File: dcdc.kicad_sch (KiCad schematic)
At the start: 72 parts, among them U2 LD1117S50TR_SOT223, U3 LD1117S33TR_SOT223, U4 ISU0205S15, U5 ISU0205S15, U6 LT3032, U7 LT3032

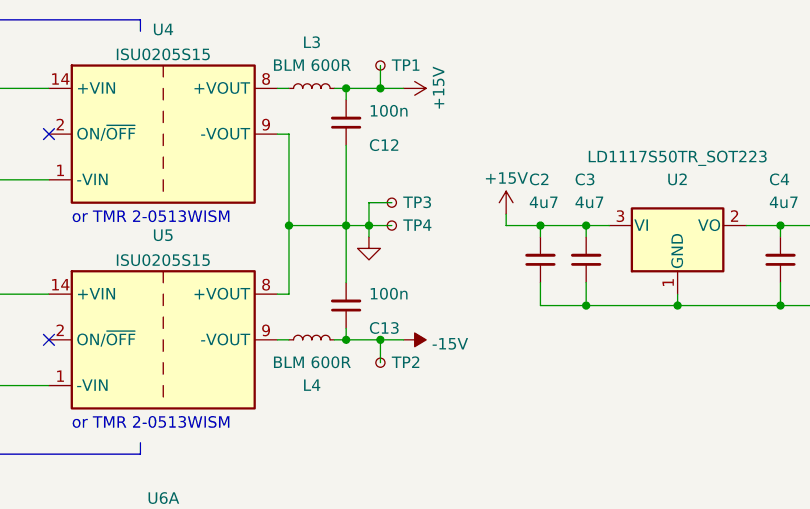
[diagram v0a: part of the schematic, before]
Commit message: Add more testpoints, make DRDY optionally open collector.
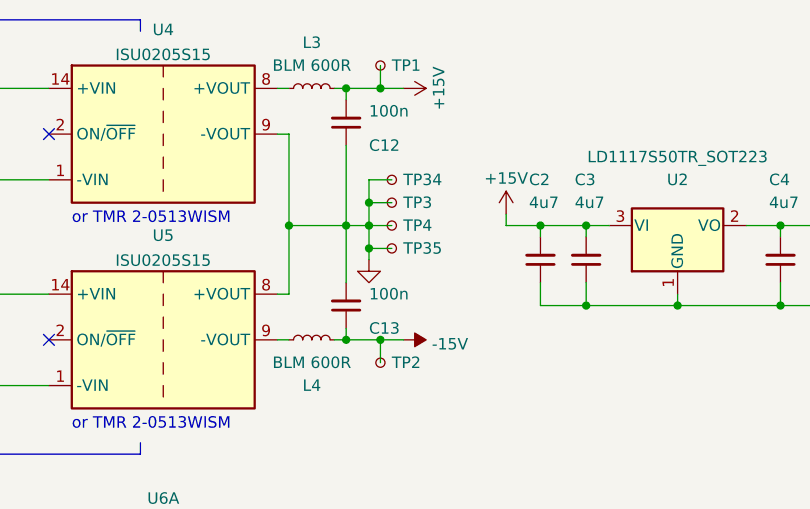
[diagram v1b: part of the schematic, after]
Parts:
- added TP34, TP35: TestPoint_Small, TestPoint:TestPoint_Pad_1.5x1.5mm, symbol Connector:TestPoint_Small
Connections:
- net GND1: now also TP34.1, TP35.1
